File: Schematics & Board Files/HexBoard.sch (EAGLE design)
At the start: 26 parts, among them X1 SSW-105-02-S-D-RA

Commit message: New board design
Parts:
- removed X1: SSW-105-02-S-D-RA, con-samtec:SSW-105-02-S-D-RA
- added XTAL: TXC-CRYSTAL, TXC:TXC-CRYSTAL
- C5: value 12p -> 2.2n
- C6: value 12p -> 1p
- C7: value 12p -> 1.5p
- C8: value 12p -> 3.9p
- U$1: value TXC-CRYSTAL -> HEADER.05"PITCH; device TXC:TXC-CRYSTAL -> Headers:HEADER.05"PITCH
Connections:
- net GND: now also U$1.P$3, U$1.P$5, U$1.P$9, XTAL.GND1, XTAL.GND2; no longer U$1.GND1, U$1.GND2, X1-3.1, X1-5.1, X1-9.1
- net N$10: now also U$1.P$2; no longer X1-2.1
- net N$7: now also U$1.P$4; no longer X1-4.1
- net N$8: now also XTAL.CRY2; no longer U$1.CRY2
- net N$9: now also XTAL.CRY1; no longer U$1.CRY1
- net VDD: now also U$1.P$1; no longer X1-1.1
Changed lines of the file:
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@@
 <part name="C1" library="adafruit" deviceset="C-US" device="C0805K" value="10u"/>
 <part name="C2" library="adafruit" deviceset="C-US" device="C0805K" value="10u"/>
-<part name="U$1" library="TXC" deviceset="TXC-CRYSTAL" device=""/>
+<part name="XTAL" library="TXC" deviceset="TXC-CRYSTAL" device=""/>
 <part name="GND2" library="supply1" deviceset="GND" device=""/>
 <part name="GND3" library="supply1" deviceset="GND" device=""/>
@@
 <part name="C4" library="adafruit" deviceset="C-US" device="C0402" value="12p"/>
 <part name="GND4" library="supply1" deviceset="GND" device=""/>
-<part name="X1" library="con-samtec" deviceset="SSW-105-02-S-D" device="-RA"/>
 <part name="VDD3" library="supply1" deviceset="VDD" device=""/>
 <part name="GND5" library="supply1" deviceset="GND" device=""/>
@@
 <part name="L1" library="CHIP_INDUCTOR" deviceset="402_CHIP_INDUCTOR" device="" value="10n"/>
 <part name="L3" library="CHIP_INDUCTOR" deviceset="402_CHIP_INDUCTOR" device="" value="3.3n"/>
-<part name="C5" library="adafruit" deviceset="C-US" device="C0402" value="12p"/>
-<part name="C6" library="adafruit" deviceset="C-US" device="C0402" value="12p"/>
-<part name="C7" library="adafruit" deviceset="C-US" device="C0402" value="12p"/>
-<part name="C8" library="adafruit" deviceset="C-US" device="C0402" value="12p"/>
+<part name="C5" library="adafruit" deviceset="C-US" device="C0402" value="2.2n"/>
+<part name="C6" library="adafruit" deviceset="C-US" device="C0402" value="1p"/>
+<part name="C7" library="adafruit" deviceset="C-US" device="C0402" value="1.5p"/>
+<part name="C8" library="adafruit" deviceset="C-US" device="C0402" value="3.9p"/>
 <part name="GND7" library="supply1" deviceset="GND" device=""/>
 <part name="GND8" library="supply1" deviceset="GND" device=""/>
@@
 <part name="VDD5" library="supply1" deviceset="VDD" device=""/>
 <part name="VDD6" library="supply1" deviceset="VDD" device=""/>
+<part name="U$1" library="Headers" deviceset="HEADER.05&quot;PITCH" device=""/>
 </parts>
 <sheets>
@@
 <instance part="C1" gate="G$1" x="38.1" y="111.76"/>
 <instance part="C2" gate="G$1" x="17.78" y="111.76"/>
-<instance part="U$1" gate="G$1" x="124.46" y="81.28" rot="R90"/>
+<instance part="XTAL" gate="G$1" x="124.46" y="81.28" rot="R90"/>
 <instance part="GND2" gate="1" x="129.54" y="53.34"/>
 <instance part="GND3" gate="1" x="129.54" y="93.98" rot="R180"/>
@@
 <instance part="C4" gate="G$1" x="99.06" y="60.96"/>
 <instance part="GND4" gate="1" x="104.14" y="50.8"/>
-<instance part="X1" gate="-1" x="175.26" y="127"/>
-<instance part="X1" gate="-2" x="195.58" y="127"/>
-<instance part="X1" gate="-3" x="175.26" y="124.46"/>
-<instance part="X1" gate="-4" x="195.58" y="124.46"/>
-<instance part="X1" gate="-5" x="175.26" y="121.92"/>
-<instance part="X1" gate="-6" x="195.58" y="121.92"/>
-<instance part="X1" gate="-7" x="175.26" y="119.38"/>
-<instance part="X1" gate="-8" x="195.58" y="119.38"/>
-<instance part="X1" gate="-9" x="175.26" y="116.84"/>
-<instance part="X1" gate="-10" x="195.58" y="116.84"/>
 <instance part="VDD3" gate="G$1" x="149.86" y="129.54"/>
-<instance part="GND5" gate="1" x="149.86" y="104.14"/>
+<instance part="GND5" gate="1" x="151.13" y="107.95" rot="R270"/>
 <instance part="R4" gate="G$1" x="124.46" y="165.1" rot="R90"/>
 <instance part="R5" gate="G$1" x="124.46" y="137.16" rot="R90"/>
@@
 <instance part="VDD5" gate="G$1" x="134.62" y="20.32"/>
 <instance part="VDD6" gate="G$1" x="101.6" y="7.62"/>
+<instance part="U$1" gate="G$1" x="219.71" y="119.38" rot="R90"/>
 </instances>
 <busses>
@@
 </segment>
 <segment>
-<pinref part="X1" gate="-1" pin="1"/>
-<wire x1="177.8" y1="127" x2="182.88" y2="127" width="0.1524" layer="91"/>
-<wire x1="182.88" y1="127" x2="182.88" y2="132.08" width="0.1524" layer="91"/>
-<wire x1="182.88" y1="132.08" x2="154.94" y2="132.08" width="0.1524" layer="91"/>
+<wire x1="203.2" y1="132.08" x2="154.94" y2="132.08" width="0.1524" layer="91"/>
 <wire x1="154.94" y1="132.08" x2="154.94" y2="124.46" width="0.1524" layer="91"/>
 <wire x1="154.94" y1="124.46" x2="149.86" y2="124.46" width="0.1524" layer="91"/>
 <pinref part="VDD3" gate="G$1" pin="VDD"/>
 <wire x1="149.86" y1="124.46" x2="149.86" y2="127" width="0.1524" layer="91"/>
+<wire x1="203.2" y1="132.08" x2="203.2" y2="104.14" width="0.1524" layer="91"/>
+<wire x1="203.2" y1="104.14" x2="210.82" y2="104.14" width="0.1524" layer="91"/>
+<pinref part="U$1" gate="G$1" pin="P$1"/>
+<junction x="210.82" y="104.14"/>
 </segment>
 <segment>
@@
 </segment>
 <segment>
-<pinref part="U$1" gate="G$1" pin="GND1"/>
+<pinref part="XTAL" gate="G$1" pin="GND1"/>
 <pinref part="GND2" gate="1" pin="GND"/>
 <wire x1="129.54" y1="55.88" x2="129.54" y2="58.42" width="0.1524" layer="91"/>
 </segment>
 <segment>
-<pinref part="U$1" gate="G$1" pin="GND2"/>
+<pinref part="XTAL" gate="G$1" pin="GND2"/>
 <pinref part="GND3" gate="1" pin="GND"/>
 <wire x1="129.54" y1="91.44" x2="129.54" y2="88.9" width="0.1524" layer="91"/>
@@
 <pinref part="GND4" gate="1" pin="GND"/>
 <wire x1="104.14" y1="55.88" x2="104.14" y2="53.34" width="0.1524" layer="91"/>
-</segment>
-<segment>
-<pinref part="X1" gate="-3" pin="1"/>
-<wire x1="177.8" y1="124.46" x2="182.88" y2="124.46" width="0.1524" layer="91"/>
-<wire x1="182.88" y1="124.46" x2="182.88" y2="121.92" width="0.1524" layer="91"/>
-<wire x1="182.88" y1="121.92" x2="182.88" y2="116.84" width="0.1524" layer="91"/>
-<wire x1="182.88" y1="116.84" x2="182.88" y2="111.76" width="0.1524" layer="91"/>
-<wire x1="182.88" y1="111.76" x2="149.86" y2="111.76" width="0.1524" layer="91"/>
-<wire x1="149.86" y1="111.76" x2="149.86" y2="106.68" width="0.1524" layer="91"/>
-<pinref part="X1" gate="-5" pin="1"/>
-<wire x1="177.8" y1="121.92" x2="182.88" y2="121.92" width="0.1524" layer="91"/>
-<pinref part="X1" gate="-9" pin="1"/>
-<wire x1="177.8" y1="116.84" x2="182.88" y2="116.84" width="0.1524" layer="91"/>
-<pinref part="GND5" gate="1" pin="GND"/>
 </segment>
 <segment>
@@
 <junction x="116.84" y="25.4"/>
 </segment>
+<segment>
+<wire x1="210.82" y1="107.95" x2="207.01" y2="107.95" width="0.1524" layer="91"/>
+<wire x1="207.01" y1="107.95" x2="207.01" y2="111.76" width="0.1524" layer="91"/>
+<pinref part="U$1" gate="G$1" pin="P$3"/>
+<pinref part="U$1" gate="G$1" pin="P$5"/>
+<wire x1="210.82" y1="111.76" x2="207.01" y2="111.76" width="0.1524" layer="91"/>
+<junction x="210.82" y="111.76"/>
+<wire x1="207.01" y1="111.76" x2="207.01" y2="119.38" width="0.1524" layer="91"/>
+<wire x1="207.01" y1="119.38" x2="210.82" y2="119.38" width="0.1524" layer="91"/>
+<wire x1="207.01" y1="107.95" x2="153.67" y2="107.95" width="0.1524" layer="91"/>
+<pinref part="GND5" gate="1" pin="GND"/>
+<pinref part="U$1" gate="G$1" pin="P$9"/>
+</segment>
 </net>
 <net name="N$8" class="0">
@@
 <wire x1="88.9" y1="93.98" x2="114.3" y2="93.98" width="0.1524" layer="91"/>
 <wire x1="114.3" y1="93.98" x2="114.3" y2="88.9" width="0.1524" layer="91"/>
-<pinref part="U$1" gate="G$1" pin="CRY2"/>
+<pinref part="XTAL" gate="G$1" pin="CRY2"/>
 <pinref part="U1" gate="G$1" pin="XC1"/>
 </segment>
@@
 <wire x1="99.06" y1="73.66" x2="104.14" y2="73.66" width="0.1524" layer="91"/>
 <wire x1="104.14" y1="73.66" x2="104.14" y2="58.42" width="0.1524" layer="91"/>
-<pinref part="U$1" gate="G$1" pin="CRY1"/>
+<pinref part="XTAL" gate="G$1" pin="CRY1"/>
 <wire x1="104.14" y1="58.42" x2="114.3" y2="58.42" width="0.1524" layer="91"/>
 <pinref part="U1" gate="G$1" pin="XC2"/>
@@
 <pinref part="R4" gate="G$1" pin="1"/>
 <wire x1="124.46" y1="157.48" x2="124.46" y2="160.02" width="0.1524" layer="91"/>
-<wire x1="124.46" y1="157.48" x2="210.82" y2="157.48" width="0.1524" layer="91"/>
-<pinref part="X1" gate="-4" pin="1"/>
-<wire x1="210.82" y1="157.48" x2="210.82" y2="124.46" width="0.1524" layer="91"/>
-<wire x1="210.82" y1="124.46" x2="198.12" y2="124.46" width="0.1524" layer="91"/>
+<wire x1="124.46" y1="157.48" x2="236.22" y2="157.48" width="0.1524" layer="91"/>
+<wire x1="236.22" y1="157.48" x2="236.22" y2="107.95" width="0.1524" layer="91"/>
+<wire x1="227.33" y1="107.95" x2="236.22" y2="107.95" width="0.1524" layer="91"/>
+<pinref part="U$1" gate="G$1" pin="P$4"/>
 </segment>
 </net>
@@
 <pinref part="R5" gate="G$1" pin="2"/>
 <wire x1="124.46" y1="144.78" x2="124.46" y2="142.24" width="0.1524" layer="91"/>
-<wire x1="124.46" y1="144.78" x2="203.2" y2="144.78" width="0.1524" layer="91"/>
-<pinref part="X1" gate="-2" pin="1"/>
-<wire x1="203.2" y1="144.78" x2="203.2" y2="127" width="0.1524" layer="91"/>
-<wire x1="203.2" y1="127" x2="198.12" y2="127" width="0.1524" layer="91"/>
-</segment>
-</net>
+<wire x1="124.46" y1="144.78" x2="229.87" y2="144.78" width="0.1524" layer="91"/>
+<wire x1="229.87" y1="144.78" x2="229.87" y2="104.14" width="0.1524" layer="91"/>
+<wire x1="229.87" y1="104.14" x2="227.33" y2="104.14" width="0.1524" layer="91"/>
+<pinref part="U$1" gate="G$1" pin="P$2"/>
+</segment>
+</net>

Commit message: Board and schematic cleanup; see email to Kris today for notes.
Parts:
- removed XTAL: TXC-CRYSTAL, TXC:TXC-CRYSTAL
- added X1: TXC-CRYSTAL, TXC:TXC-CRYSTAL
- C1, C2: device adafruit:C-USC0805K -> rcl:C-EUC0805
- C10, C11, C12, C3, C4, C5, C6, C7, C8, C9: device adafruit:C-USC0402 -> rcl:C-EUC0402
- C13: device adafruit:C-USC0603K -> rcl:C-EUC0402
- L1, L2, L3: device CHIP_INDUCTOR:402_CHIP_INDUCTOR -> rcl_custom:L-US0402-B-NOSILK
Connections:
- net N$10 renamed !RESET
- net N$7 renamed SWD
- net GND: now also X1.GND1, X1.GND2; no longer XTAL.GND1, XTAL.GND2
- net N$11: now also L1.2, L2.1; no longer L1.1, L2.2
- net N$15: now also L2.2; no longer L2.1
- net N$17: now also L1.1; no longer L1.2
- net N$8: now also X1.CRY2; no longer XTAL.CRY2
- net N$9: now also X1.CRY1; no longer XTAL.CRY1
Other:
- moved on the sheet: C1, C10, C11, C12, C13, C2, C3, C4, C5, C6, C7, C8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

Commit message: Latest code latest board and schematic updated maker guide
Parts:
- removed X1: TXC-CRYSTAL, TXC:TXC-CRYSTAL
- added U$2: TXC-CRYSTAL, TXC:TXC-CRYSTAL
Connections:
- net GND: now also U$2.G1, U$2.G2; no longer X1.GND1, X1.GND2
- net N$8: now also U$2.X1; no longer X1.CRY2
- net N$9: now also U$2.X2; no longer X1.CRY1
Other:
- note added: "Battery Circuit"
- note added: "Matching Network"
- note added: "NRF51822 or NRF51422"
- note added: "Programming Header"
- moved on the sheet: C10, C12, C3, C4, C5, C6, C7, C8, L1, L2, L3, R4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

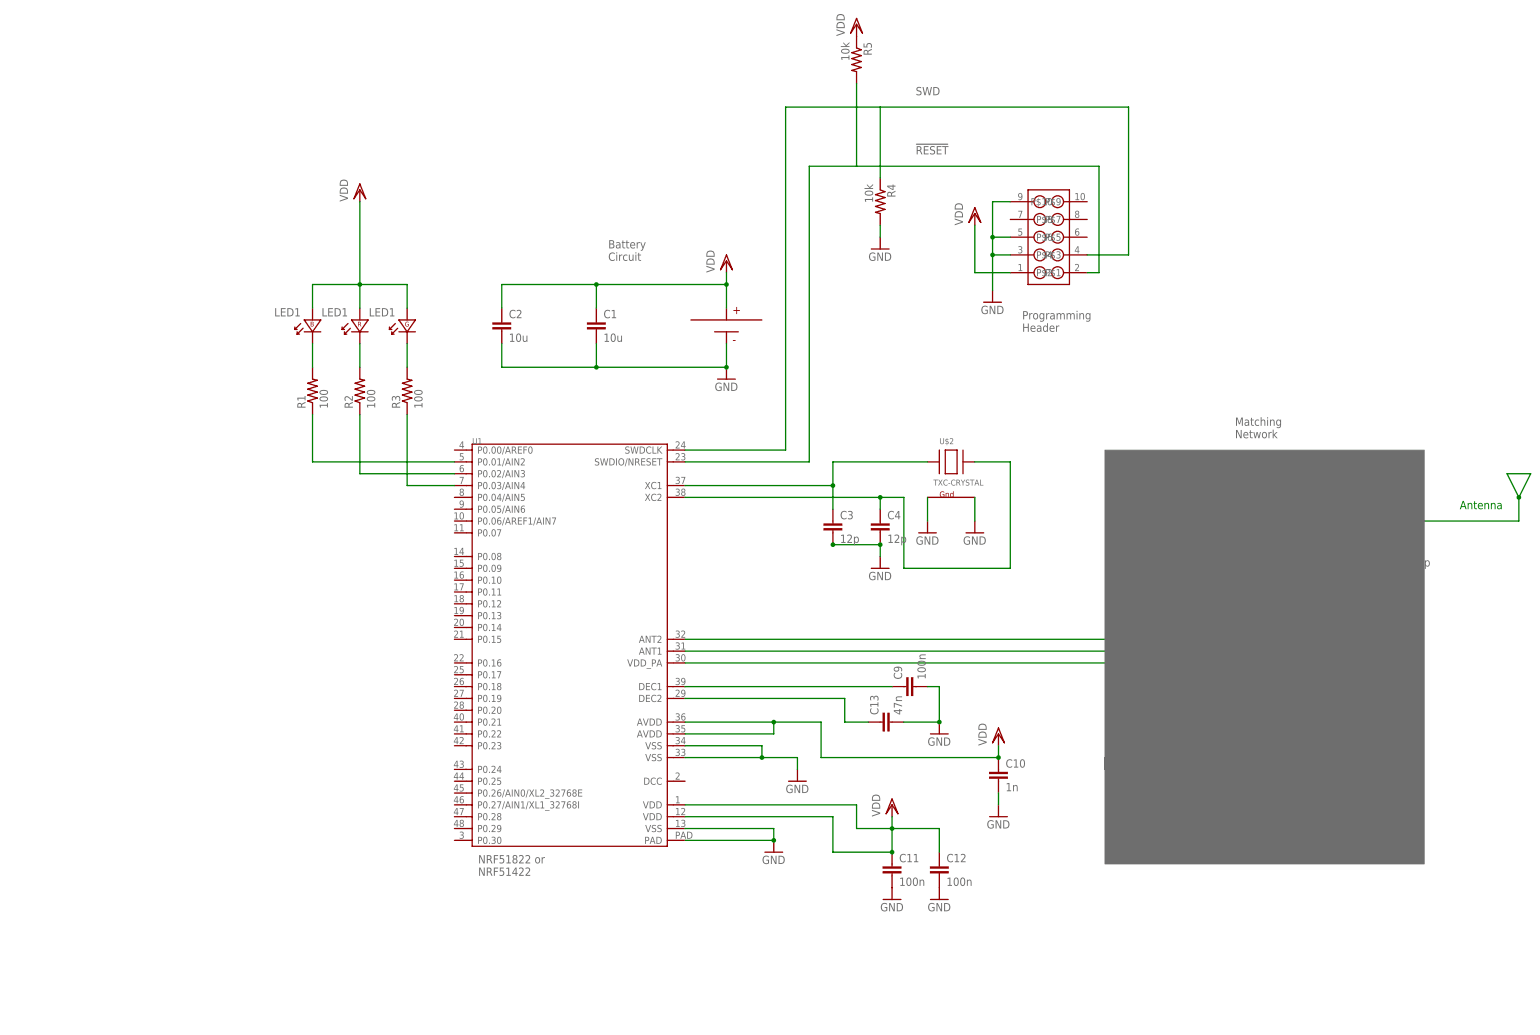
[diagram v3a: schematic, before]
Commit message: OCD cleaned up of schematic -- nothing different, just prettyness. Cleaned up TNAMES layer a bit on board, checked DRC, moved a few vias... it's good to go. Sending off to OSH Parkgit add HexBoard.brd HexBoard.sch11!
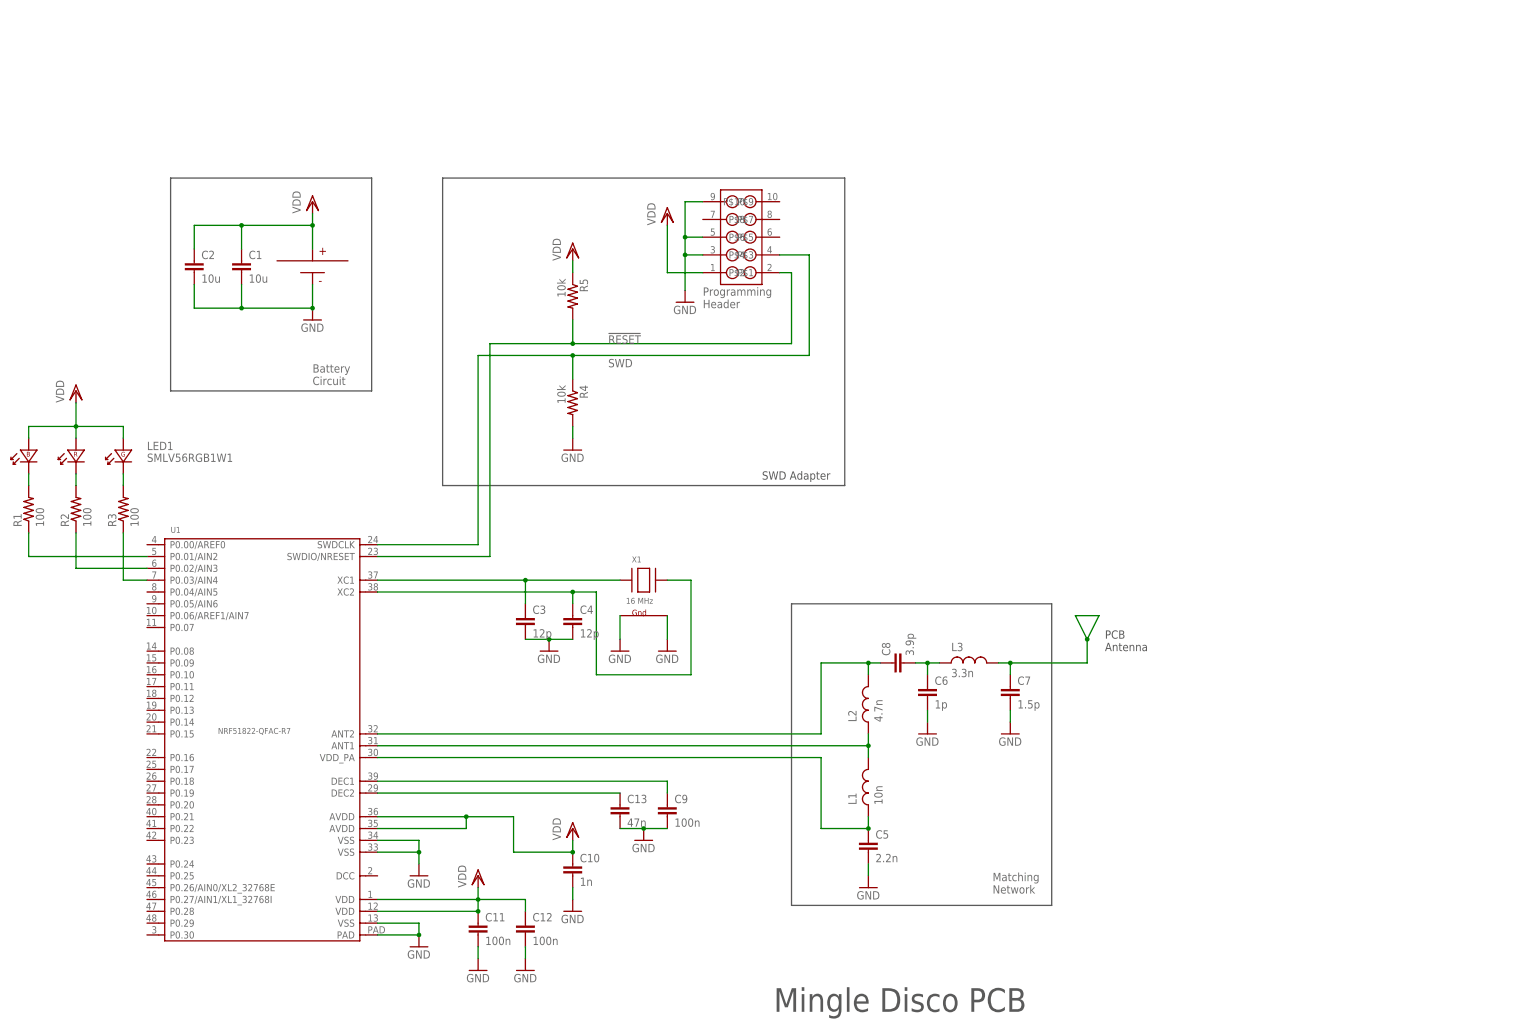
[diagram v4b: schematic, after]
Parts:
- removed U$2: TXC-CRYSTAL, TXC:TXC-CRYSTAL
- added X1: 16 MHz, TXC:TXC-CRYSTAL
- LED1: value (none) -> SMLV56RGB1W1
- U1: value (none) -> NRF51822-QFAC-R7
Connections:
- net GND: now also X1.G1, X1.G2; no longer U$2.G1, U$2.G2
- net N$8: now also X1.X1; no longer U$2.X1
- net N$9: now also X1.X2; no longer U$2.X2
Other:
- note added: "Mingle Disco PCB"
- note added: "PCB Antenna"
- note added: "SWD Adapter"
- note removed: "Antenna"
- note removed: "NRF51822 or NRF51422"
- moved on the sheet: C1, C10, C11, C12, C13, C2, C3, C4, C5, C6, C7, C8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
